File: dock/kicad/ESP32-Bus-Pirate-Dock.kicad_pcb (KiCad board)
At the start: 4 copper layers, 80 x 73.8 mm, 49 parts, among them CN1 HX25418-10WA, J1 Conn_01x22, J2 Conn_01x22, J3 Conn_01x10V, J4 Conn_01x22, J5 Conn_01x22, J6 Conn_01x22, J7 Conn_02x03, J8 TC2050, Q1 2SK2009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

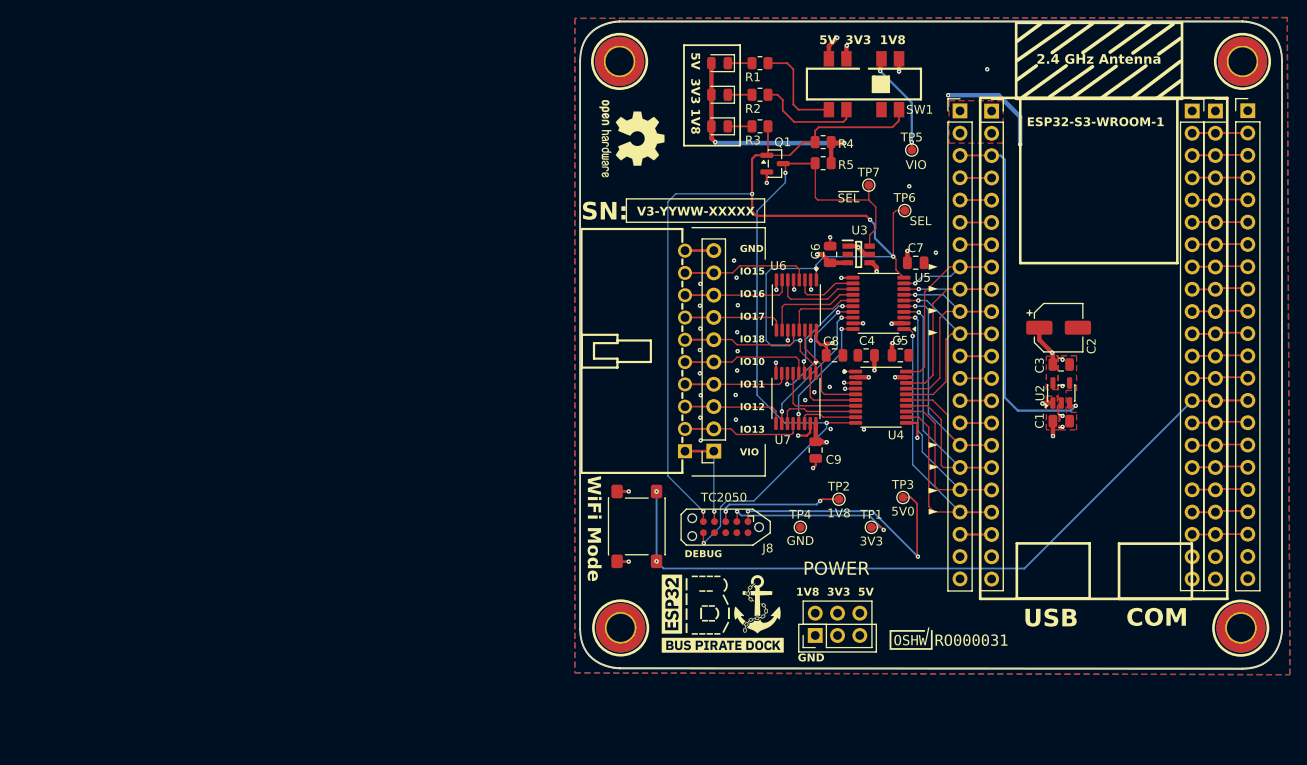
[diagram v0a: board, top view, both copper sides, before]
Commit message: Length matching on translated pins
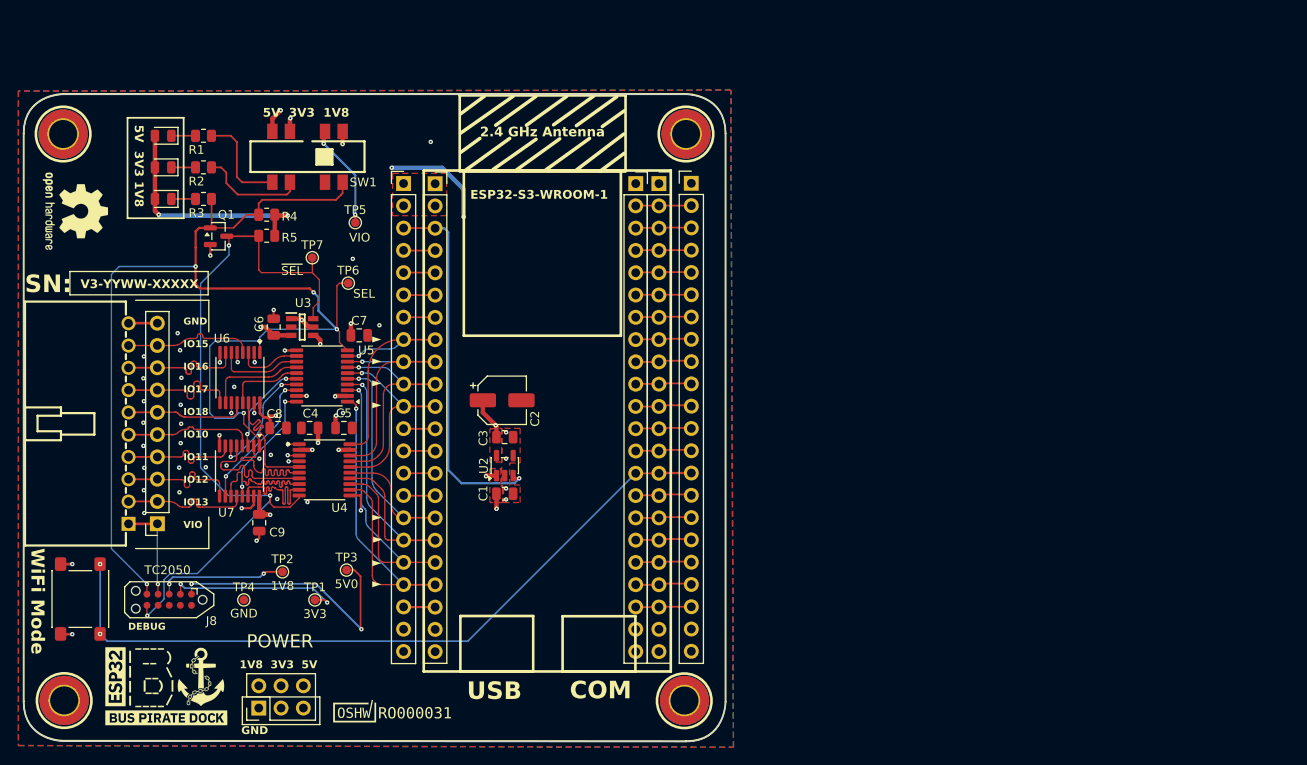
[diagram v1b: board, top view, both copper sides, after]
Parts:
- moved C2 64.0 mm to (114.8, 103.4)
- moved C4 64.0 mm to (92.9, 106.6)
- moved C9 64.0 mm to (87.1, 117.4)
- moved G*** 64.0 mm to (76.5, 136.1)
- moved H1 64.0 mm to (135.6, 137.6)
- moved J4 64.0 mm to (136.4, 78.7)
- moved J5 64.0 mm to (132.7, 78.7)
- moved J6 64.0 mm to (130.0, 78.7)
- moved R4 64.0 mm to (88.0, 82.3)
- moved R5 64.0 mm to (88.0, 84.7)
- moved SW1 64.0 mm to (92.6, 75.7)
- moved TP1 64.0 mm to (93.5, 126.2)
- moved TP4 64.0 mm to (85.4, 126.2)
- moved U7 64.0 mm to (84.9, 111.5)
- moved C1 64.0 mm to (115.1, 114.1)
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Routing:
- net /Voltage Level Translator/IO13_L: track 6.88 -> 15.7 mm
- net /Voltage Level Translator/IO10_L: track 8.01 -> 15.6 mm
- net /Voltage Level Translator/IO12_L: track 9.41 -> 15.6 mm
- net /Voltage Level Translator/IO11_L: track 10.7 -> 15.7 mm
- net /Voltage Level Translator/IO18_L: track 12.2 -> 15.7 mm
- net IO17: track 11.6 -> 14.9 mm
- net IO12: track 12.0 -> 14.9 mm
- net IO11: track 12.1 -> 14.9 mm
- net IO16: track 12.6 -> 14.9 mm
- net /Voltage Level Translator/~{SEL}: track 84.3 -> 86.1 mm
- net /Voltage Level Translator/IO15_L: track 13.9 -> 15.5 mm
- net /Voltage Level Translator/IO17_L: track 11.6 -> 12.9 mm
- net IO13: track 13.7 -> 14.9 mm
- net IO18: track 14.1 -> 15.0 mm
- net GND: vias 40 -> 42
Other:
- board text added: "#000000F2"
- board text added: "#808080FF"
- board text added: "0"
- board text added: "0 mm"
- board text added: "0,01 mm"
- board text added: "0,02"
- board text added: "0,035 mm"
- board text added: "0,1 mm"
- board text added: "1"
- board text added: "1,24 mm"
- board text added: "3,3"
- board text added: "4,5"
- board text added: "B.Cu"
- board text added: "B.Mask"
- board text added: "B.Paste"
- board text added: "B.Silkscreen"
- board text added: "Bottom Silk Screen"
- board text added: "Bottom Solder Mask"
- board text added: "Bottom Solder Paste"
- board text added: "Color"
- board text added: "Dielectric"
- board text added: "Epsilon R"
- board text added: "F.Cu"
- board text added: "F.Mask"
- board text added: "F.Paste"
- board text added: "F.Silkscreen"
- board text added: "FR4"
- board text added: "In1.Cu"
- board text added: "In2.Cu"
- board text added: "Layer Name"
- board text added: "Loss Tangent"
- board text added: "Material"
- board text added: "Not specified"
- board text added: "Thickness (mm)"
- board text added: "Top Silk Screen"
- board text added: "Top Solder Mask"
- board text added: "Top Solder Paste"
- board text added: "Type"
- board text added: "White"
- board text added: "copper"
- board text added: "core"
- board text added: "prepreg"
